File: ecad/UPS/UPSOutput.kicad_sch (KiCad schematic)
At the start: 32 parts, among them J3 USB_C_Receptacle_USB2.0_16P, Q3 IRLR7843TRPBF, SW3 SW_DPDT_x2, U2 MPQ5031GRE-0001-AEC1-P, U3 L78L05_SOT89

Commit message: Couple missing footprints added, Need to look into USB route, make sure voltage regulator is fine as is
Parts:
- C64: footprint (none) -> Capacitor_SMD:C_0603_1608Metric_Pad1.08x0.95mm_HandSolder
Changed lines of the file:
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@@
 			)
 		)
-		(property "Footprint" ""
+		(property "Footprint" "Capacitor_SMD:C_0603_1608Metric_Pad1.08x0.95mm_HandSolder"
 			(at 174.9552 43.18 0)
 			(hide yes)

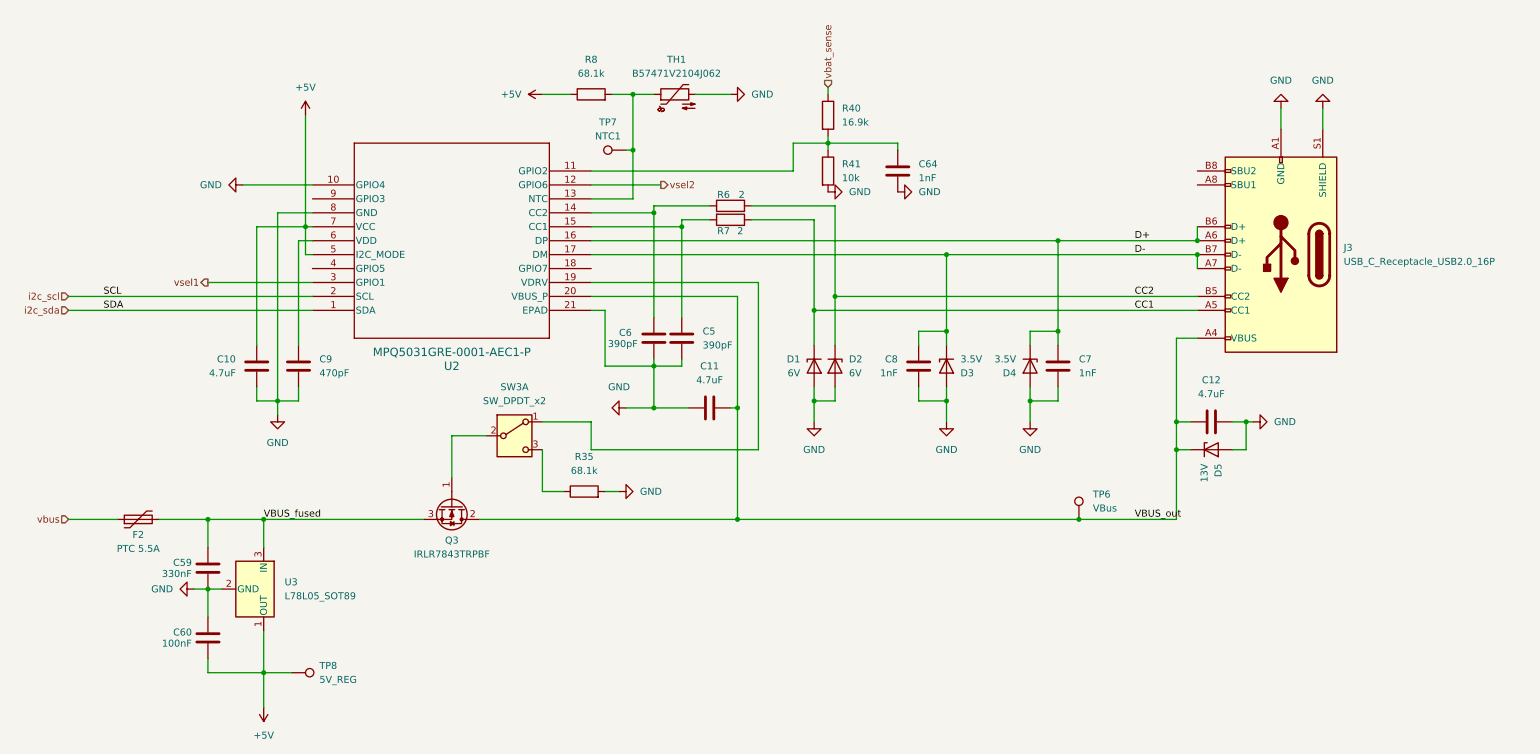
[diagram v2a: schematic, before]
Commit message: Final schematic, added fan, shrunk board down about 25%
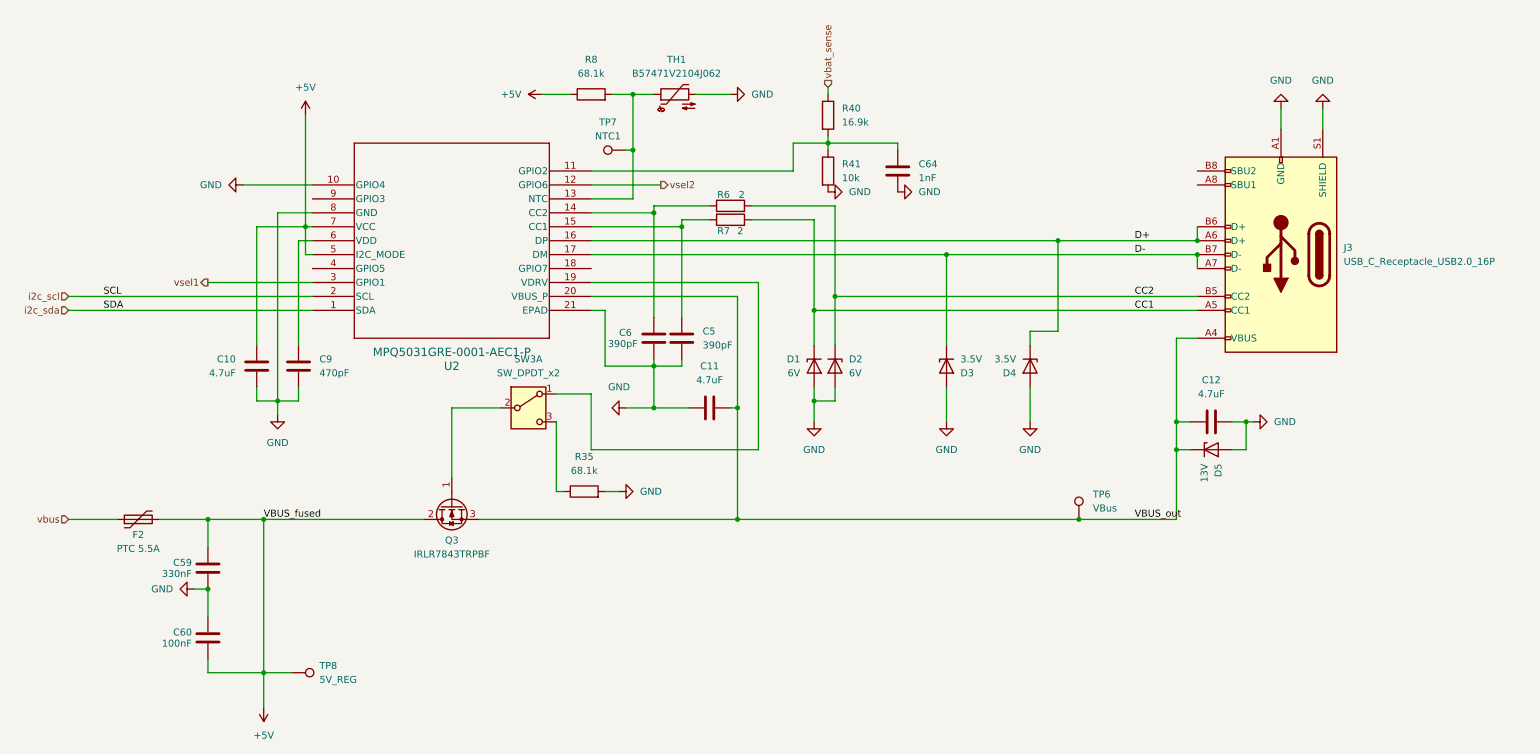
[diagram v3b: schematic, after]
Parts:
- removed C7, C8: 1nF, Capacitor_SMD:C_0603_1608Metric_Pad1.08x0.95mm_HandSolder, symbol Device:C
- removed U3: L78L05_SOT89, Package_TO_SOT_SMD:SOT-89-3, symbol Regulator_Linear:L78L05_SOT89
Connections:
- net +5V: now also C59.1, F2.2, Q3.2 (D)
- net VBUS_out: now also Q3.3 (S); no longer Q3.2 (D)
- removed net VBUS_fused: C59.1, F2.2, Q3.3 (S)
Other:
- moved on the sheet: Q3, SW3A
